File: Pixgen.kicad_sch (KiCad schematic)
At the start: 10 parts, among them U601 74HC166, U602 74HC574, U603 27C64, U604 74HC574, U605 GAL22V10

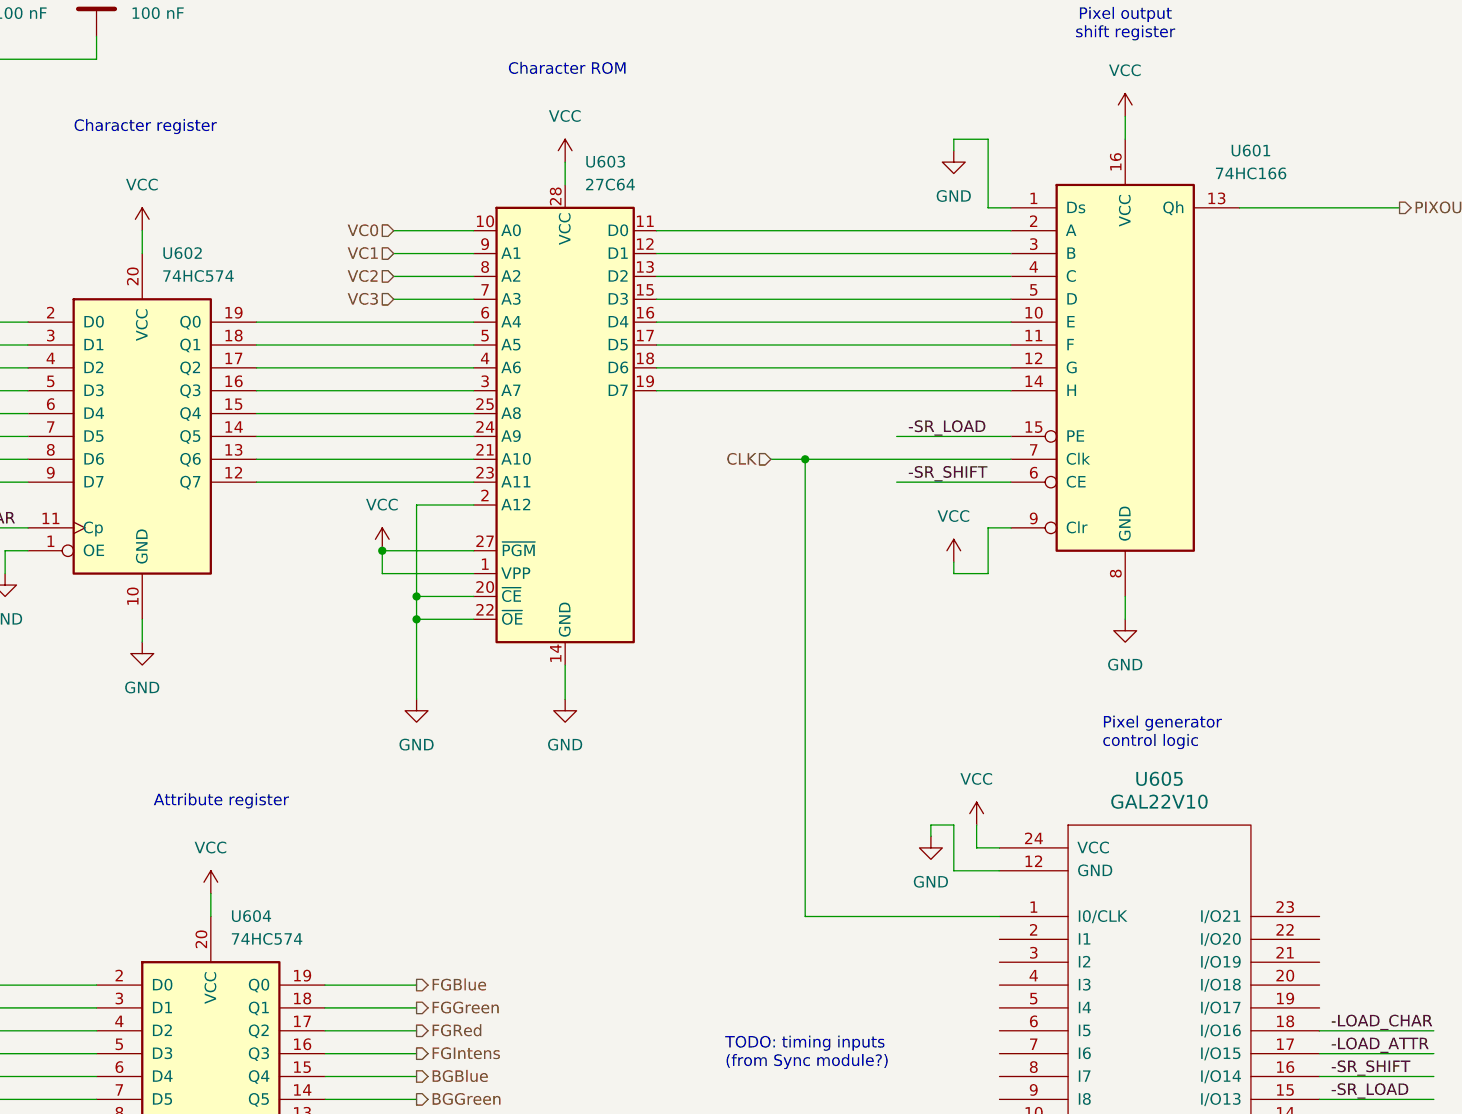
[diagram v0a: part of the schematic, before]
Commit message: chips driven by GAL or memory need to be 74HCT
I forgot that GALs only guarantee 2.4V as the minimum
output high voltage. Bleh.
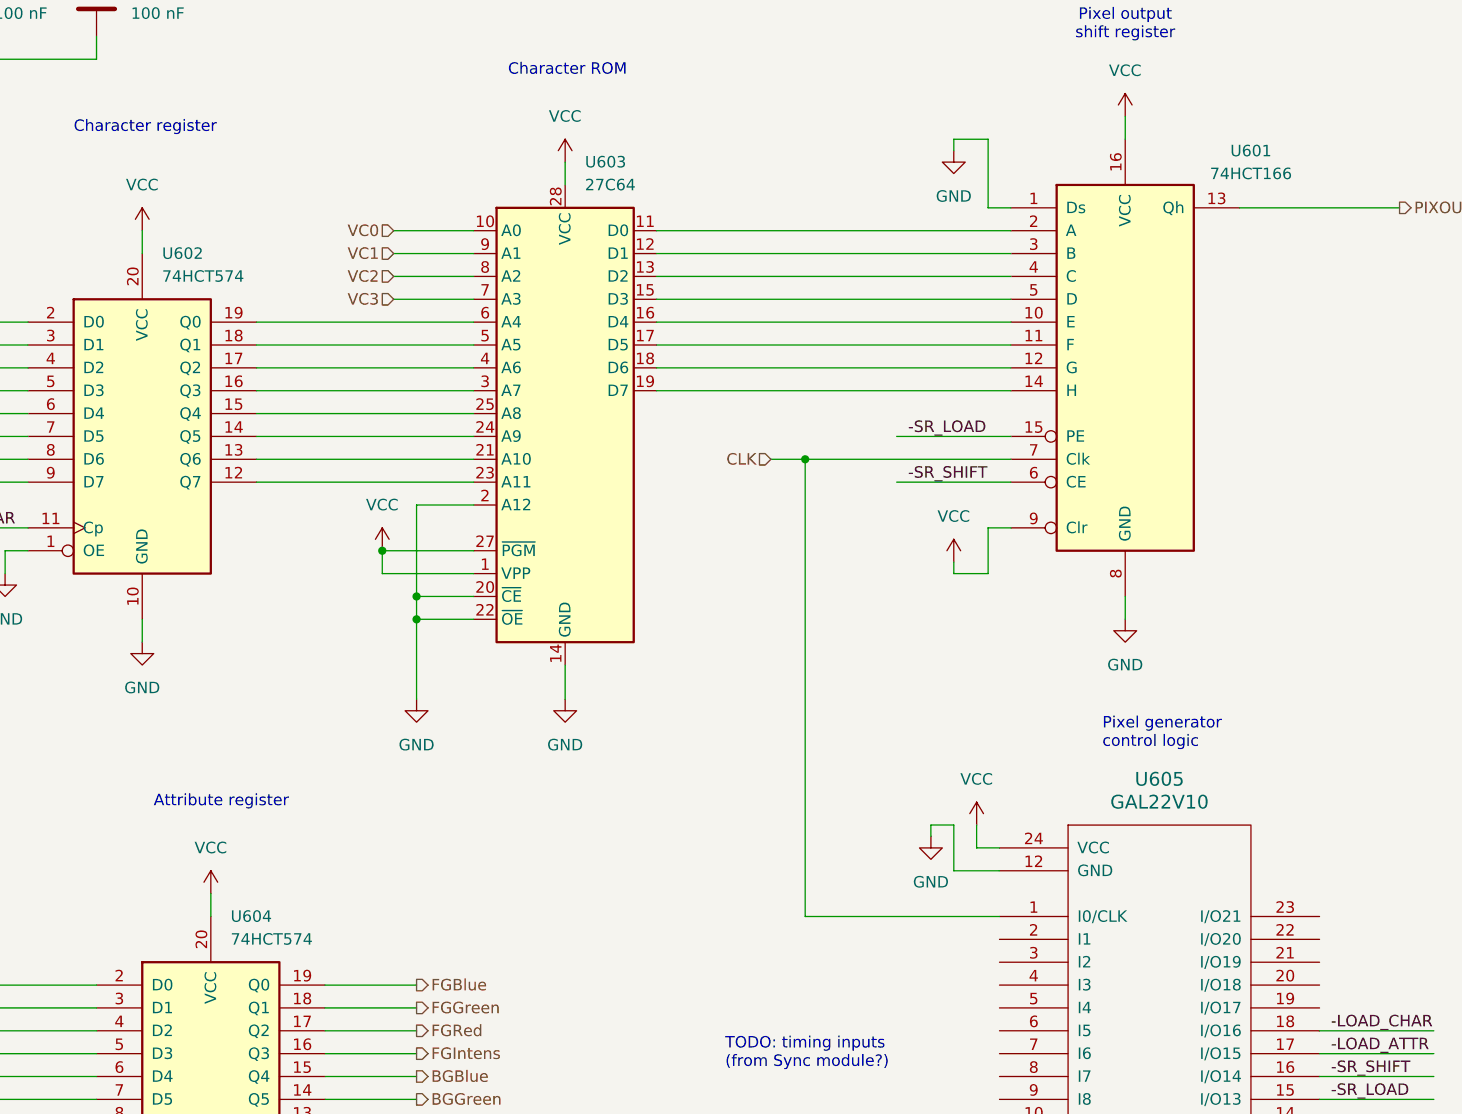
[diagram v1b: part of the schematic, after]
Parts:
- U601: value 74HC166 -> 74HCT166
- U602, U604: value 74HC574 -> 74HCT574
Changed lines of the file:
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@@
 			)
 		)
-		(property "Value" "74HC574"
+		(property "Value" "74HCT574"
 			(at 88.5541 60.96 0)
 			(effects
@@
 			)
 		)
-		(property "Value" "74HC166"
+		(property "Value" "74HCT166"
 			(at 209.55 49.5614 0)
 			(effects
@@
 			)
 		)
-		(property "Value" "74HC574"
+		(property "Value" "74HCT574"
 			(at 96.1741 134.62 0)
 			(effects

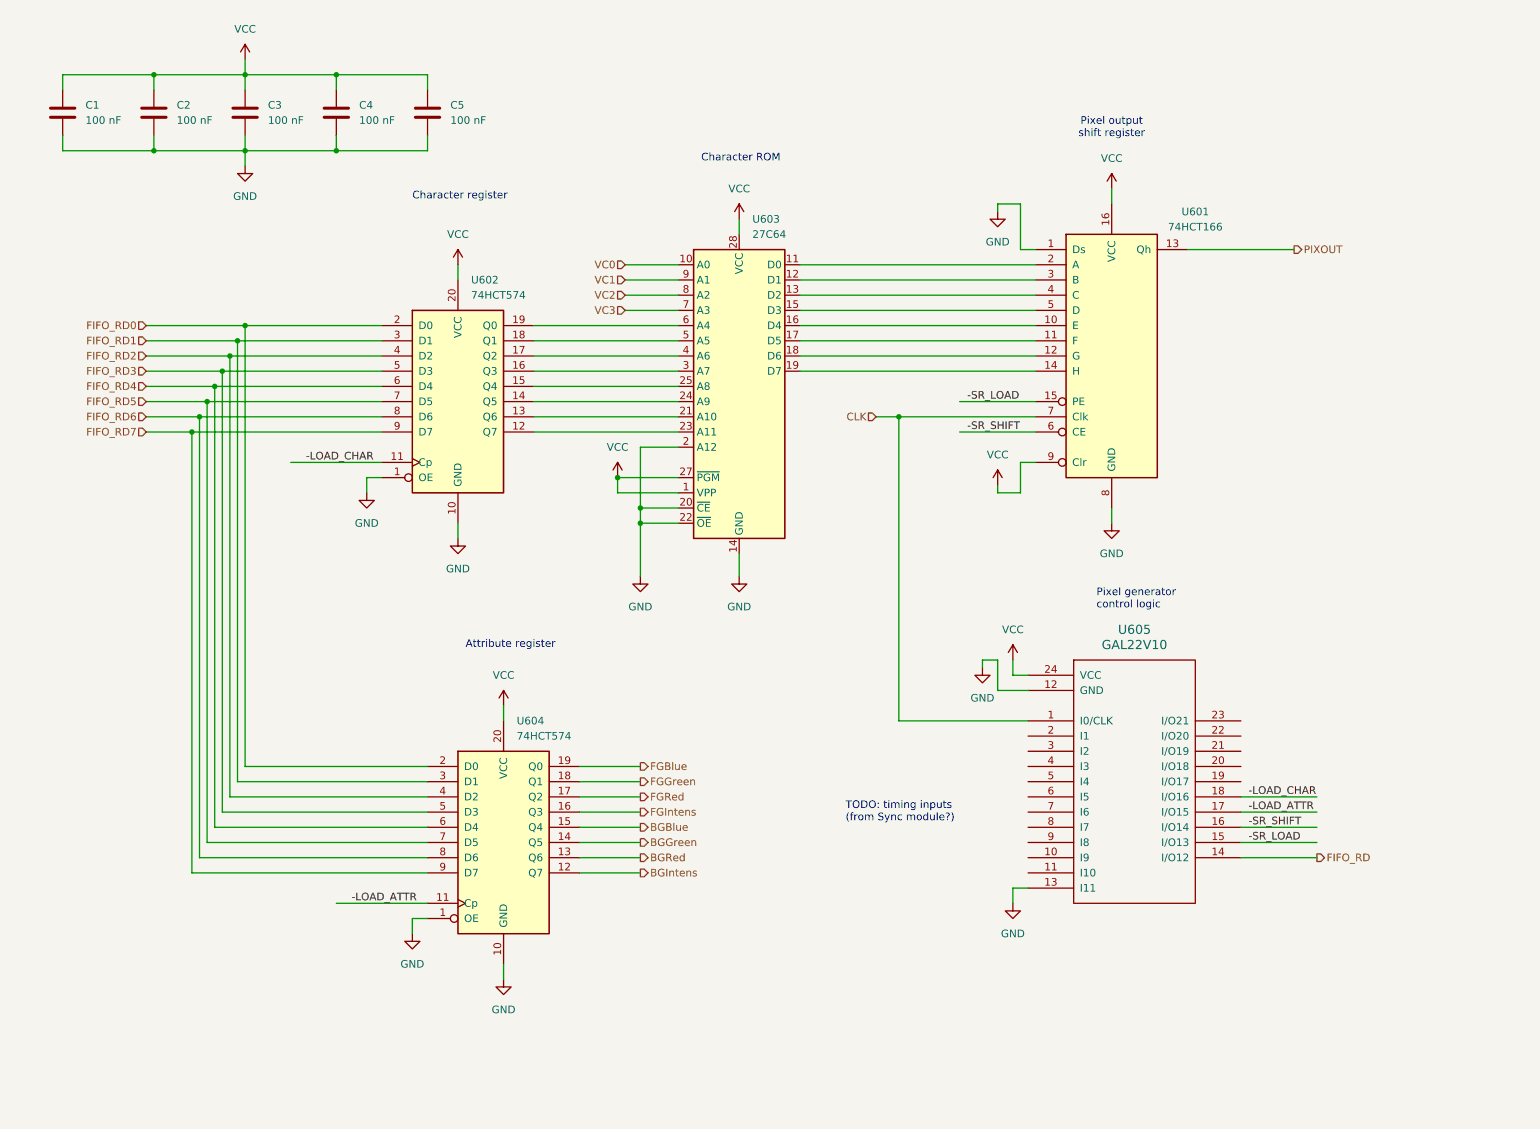
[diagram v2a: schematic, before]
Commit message: use 27SF512 for char ROM, GAL22V10 for shift reg
The 27SF512 is the fastest programmable ROM I have,
at 70 ns, so in theory could produce valid character
pixel row data after only two clock cycles.
It's a bit less "authentic" than, let's say, a
27C256-70, but I don't have any of those, and
the T48 should be able to program the 27SF512.

Originally I was going to use a '166 shift register
for the pixel output, but the 74ACT166 is virtually
nonexistent. Apparently Hitachi made them (there's a
datasheet), but I can't find any to buy. A GAL22V10
can easily be a shift register, so no worries there.
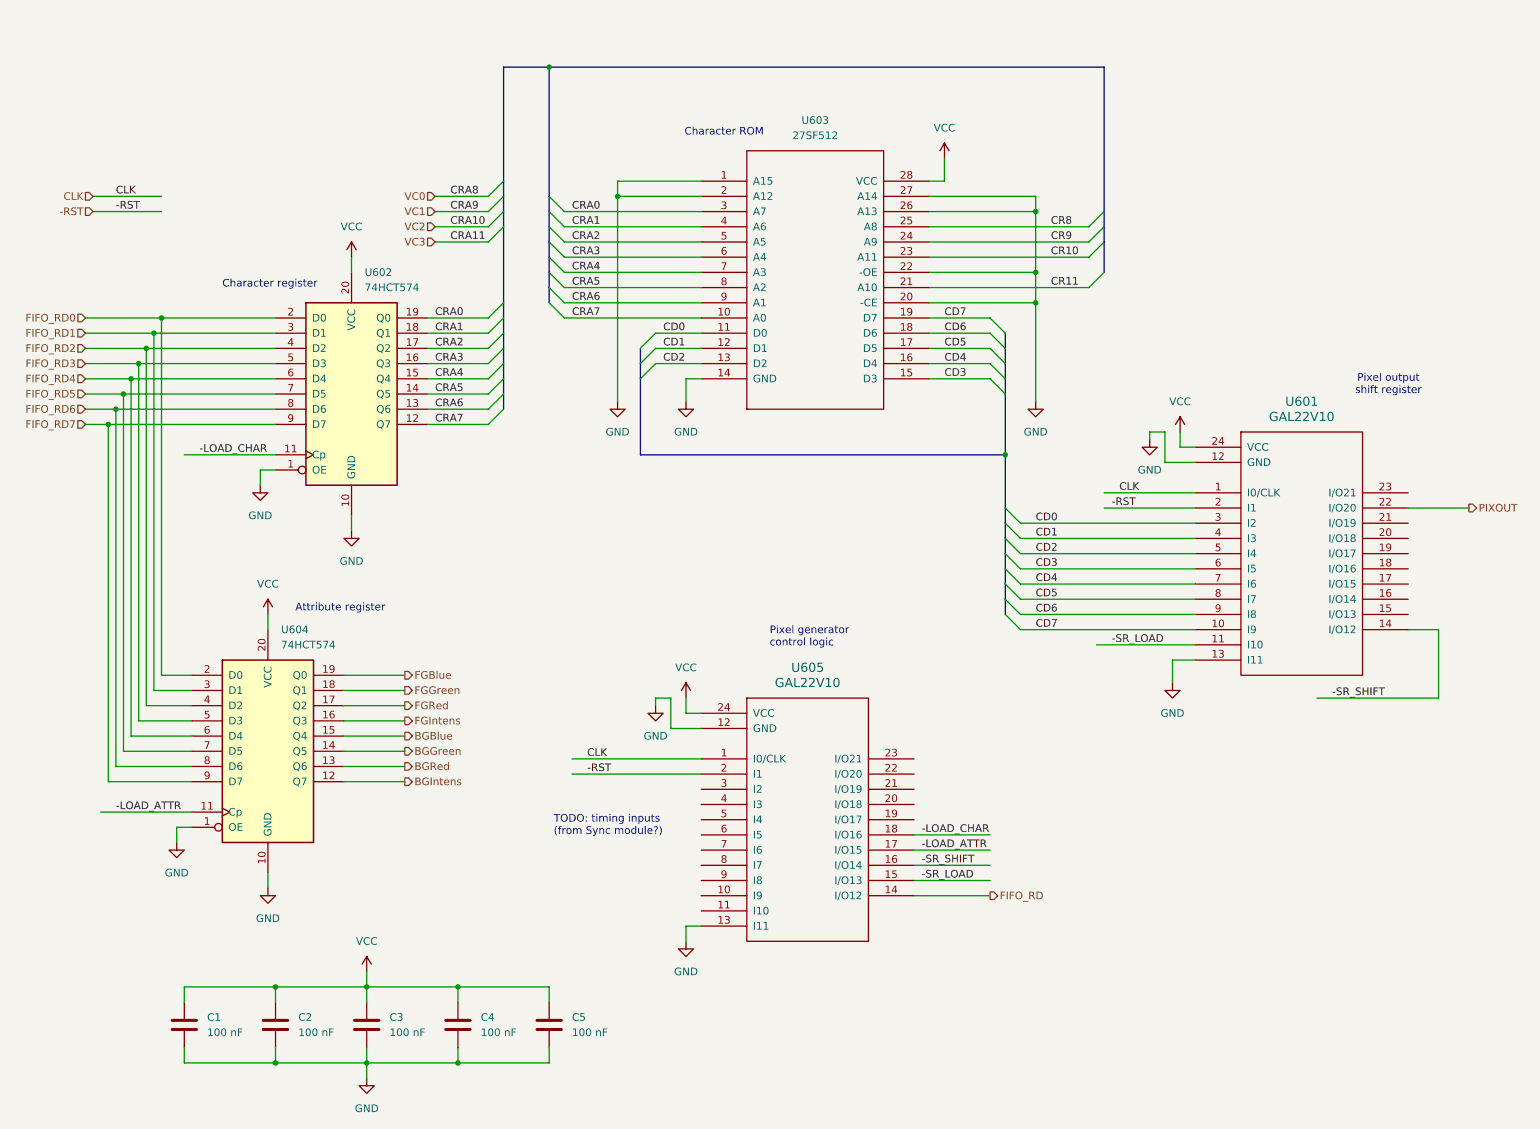
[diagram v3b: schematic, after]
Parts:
- removed U601: 74HCT166, symbol 74xx:74LS166
- removed U603: 27C64, Package_DIP:DIP-28_W15.24mm, symbol Memory_EPROM:27C64
- added U601: GAL22V10, symbol ya68k:GAL22V10
- added U603: 27SF512, MODULE, symbol 27SF512:27SF512
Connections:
- net -SR_LOAD: now also U601.11 (I10)
- net -SR_SHIFT: now also U601.14 (I/O12)
- net CLK: now also U601.1 (I0/CLK)
- net GND: now also U601.12 (GND), U601.13 (I11), U603.1 (A15), U603.14 (GND), U603.2 (A12), U603.20 (-CE), U603.22 (-OE), U603.26 (A13), U603.27 (A14)
- net PIXOUT: now also U601.22 (I/O20)
- net VCC: now also U601.24 (VCC), U603.28 (VCC)
- net CRA7: now reaches U602.12 (Q7)
- net CRA7: now also U603.10 (A0)
- net CRA6: now reaches U602.13 (Q6)
- net CRA6: now also U603.9 (A1)
- net CRA5: now reaches U602.14 (Q5)
- net CRA5: now also U603.8 (A2)
- net CRA4: now reaches U602.15 (Q4)
- net CRA4: now also U603.7 (A3)
- net CRA3: now reaches U602.16 (Q3)
- net CRA3: now also U603.6 (A4)
- net CRA2: now reaches U602.17 (Q2)
- net CRA2: now also U603.5 (A5)
- net CRA1: now reaches U602.18 (Q1)
- net CRA1: now also U603.4 (A6)
- net CRA0: now reaches U602.19 (Q0)
- net CRA0: now also U603.3 (A7)
- net -RST: now reaches U605.2 (I1)
- net -RST: now also U601.2 (I1)
- new net CD0: U601.3 (I2), U603.11 (D0)
- new net CD1: U601.4 (I3), U603.12 (D1)
- new net CD2: U601.5 (I4), U603.13 (D2)
- new net CD3: U601.6 (I5), U603.15 (D3)
- new net CD4: U601.7 (I6), U603.16 (D4)
- new net CD5: U601.8 (I7), U603.17 (D5)
- new net CD6: U601.9 (I8), U603.18 (D6)
- new net CD7: U601.10 (I9), U603.19 (D7)
- new net CR10: U603.23 (A11)
- new net CR11: U603.21 (A10)
- new net CR8: U603.25 (A8)
- new net CR9: U603.24 (A9)
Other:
- moved on the sheet: C1, C2, C3, C4, C5, U602, U604, U605

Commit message: use upper bits of bank reg to select font
With 64 KB of font memory, this means that we can
have 8 different fonts.

Also cleaned up a few issues in the pixel generator
module.
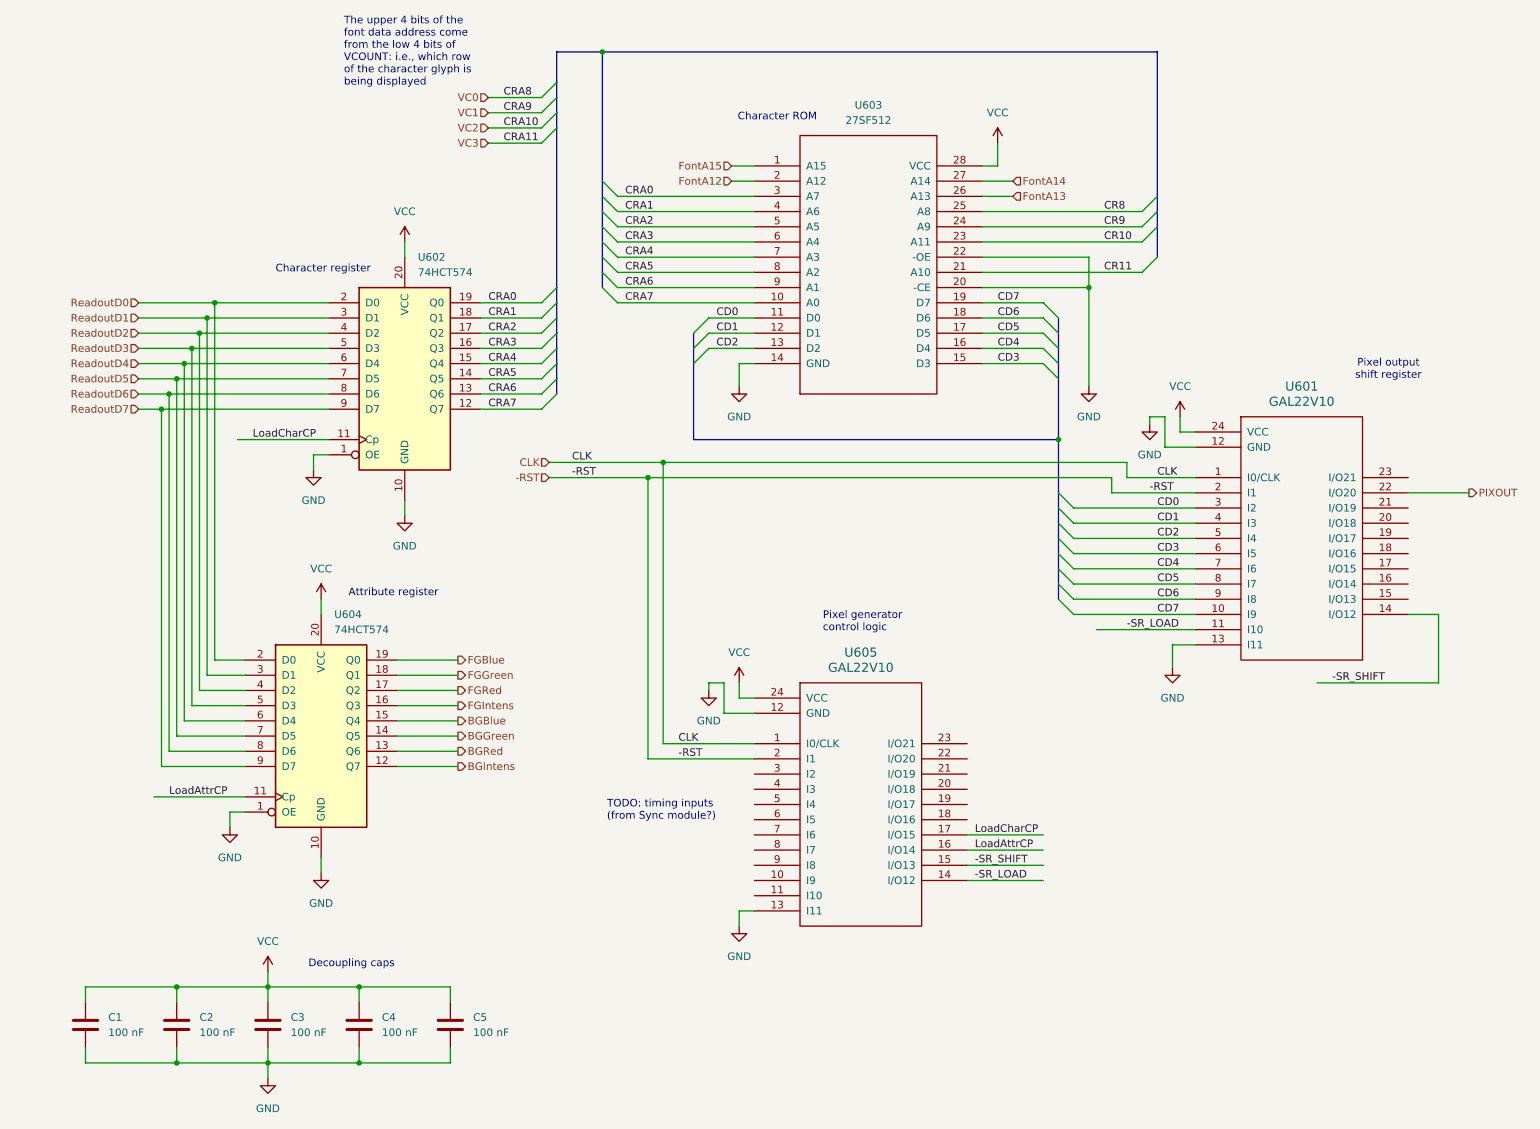
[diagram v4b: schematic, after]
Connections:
- net FIFO_RD is gone; now on net -SR_LOAD: U605.14 (I/O12)
- net -SR_LOAD: no longer U605.15 (I/O13)
- net -SR_SHIFT: now also U605.15 (I/O13); no longer U605.16 (I/O14)
- net GND: no longer U603.1 (A15), U603.2 (A12), U603.26 (A13), U603.27 (A14)
- net -LOAD_ATTR renamed LoadAttrCP
- net LoadAttrCP: now also U605.16 (I/O14); no longer U605.17 (I/O15)
- net -LOAD_CHAR: no longer names the net of U605.18 (I/O16)
- net -LOAD_CHAR: no longer U602.11 (Cp)
- net FIFO_RD0 renamed ReadoutD0
- net FIFO_RD1 renamed ReadoutD1
- net FIFO_RD2 renamed ReadoutD2
- net FIFO_RD3 renamed ReadoutD3
- net FIFO_RD4 renamed ReadoutD4
- net FIFO_RD5 renamed ReadoutD5
- net FIFO_RD6 renamed ReadoutD6
- net FIFO_RD7 renamed ReadoutD7
- new net FontA12: U603.2 (A12)
- new net FontA13: U603.26 (A13)
- new net FontA14: U603.27 (A14)
- new net FontA15: U603.1 (A15)
- new net LoadCharCP: U602.11 (Cp), U605.17 (I/O15)
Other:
- note added: "Decoupling caps"
- note added: "The upper 4 bits of the font data address come from the low 4 bits of VCOUNT: i.e., which row of the character glyph is being displayed"
- title: Pixel output -> Pixel generation
- moved on the sheet: C1, C2, C3, C4, C5, U601, U602, U603, U604, U605
